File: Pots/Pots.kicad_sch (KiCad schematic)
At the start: 10 parts, among them J101 Conn_02x05_Odd_Even

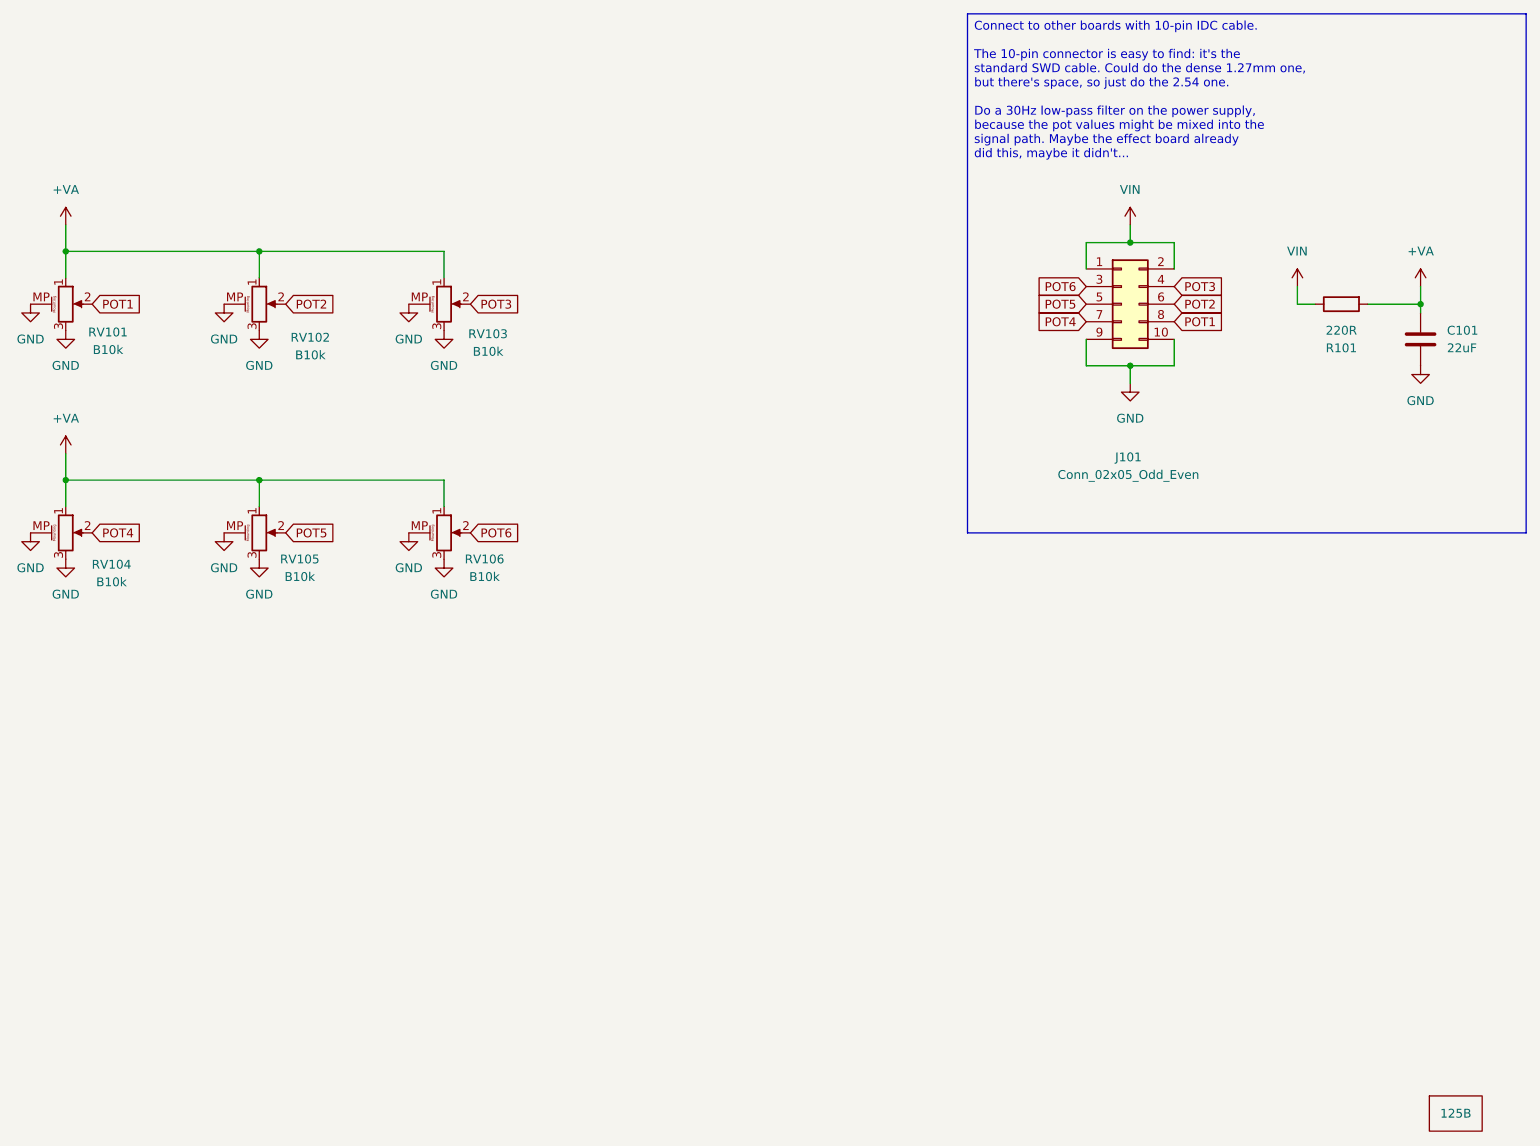
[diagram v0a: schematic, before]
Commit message: Move 3d models to footprint directory
I tried to deal with the kicad path handling with a 'TOPLEVEL'
environment variable, but it worked horribly badly and got out of sync
because kicad didn't really integrate very well with it.

So just live with the fact that you can only have per-project paths for
the symbol and footprint libraries, not for the 3D models.  kicad does
have the notion of "3D model paths", but they aren't per project.

It looks like the way to keep kicad happy and avoid too much confusion
is to just make the 3D models be part of the footprint library, and put
the STEP files in the same path.  I'll keep the original openscad models
in the 'Models' (and 'Enclosures') directories.

Let's see if this fixes my issues.

Also, this mixes in various other edits to the 1590B footprint in
particular, since I couldn't keep the regularly scheduled kicad noise
separate from the 'move things around' noise.  kicad likes to randomly
update the uuid's of various parts as something changes (or, as I
sometimes feel, even if nothing changes).

So this is not a particularly clean commit: this also moves the pot
locations up by 5mm in the 1590B enclosure because that's what I was
looking at when the potentiometer board stopped showing 3d models due to
path confusion.

Signed-off-by: Linus Torvalds <torvalds@linux-foundation.org>
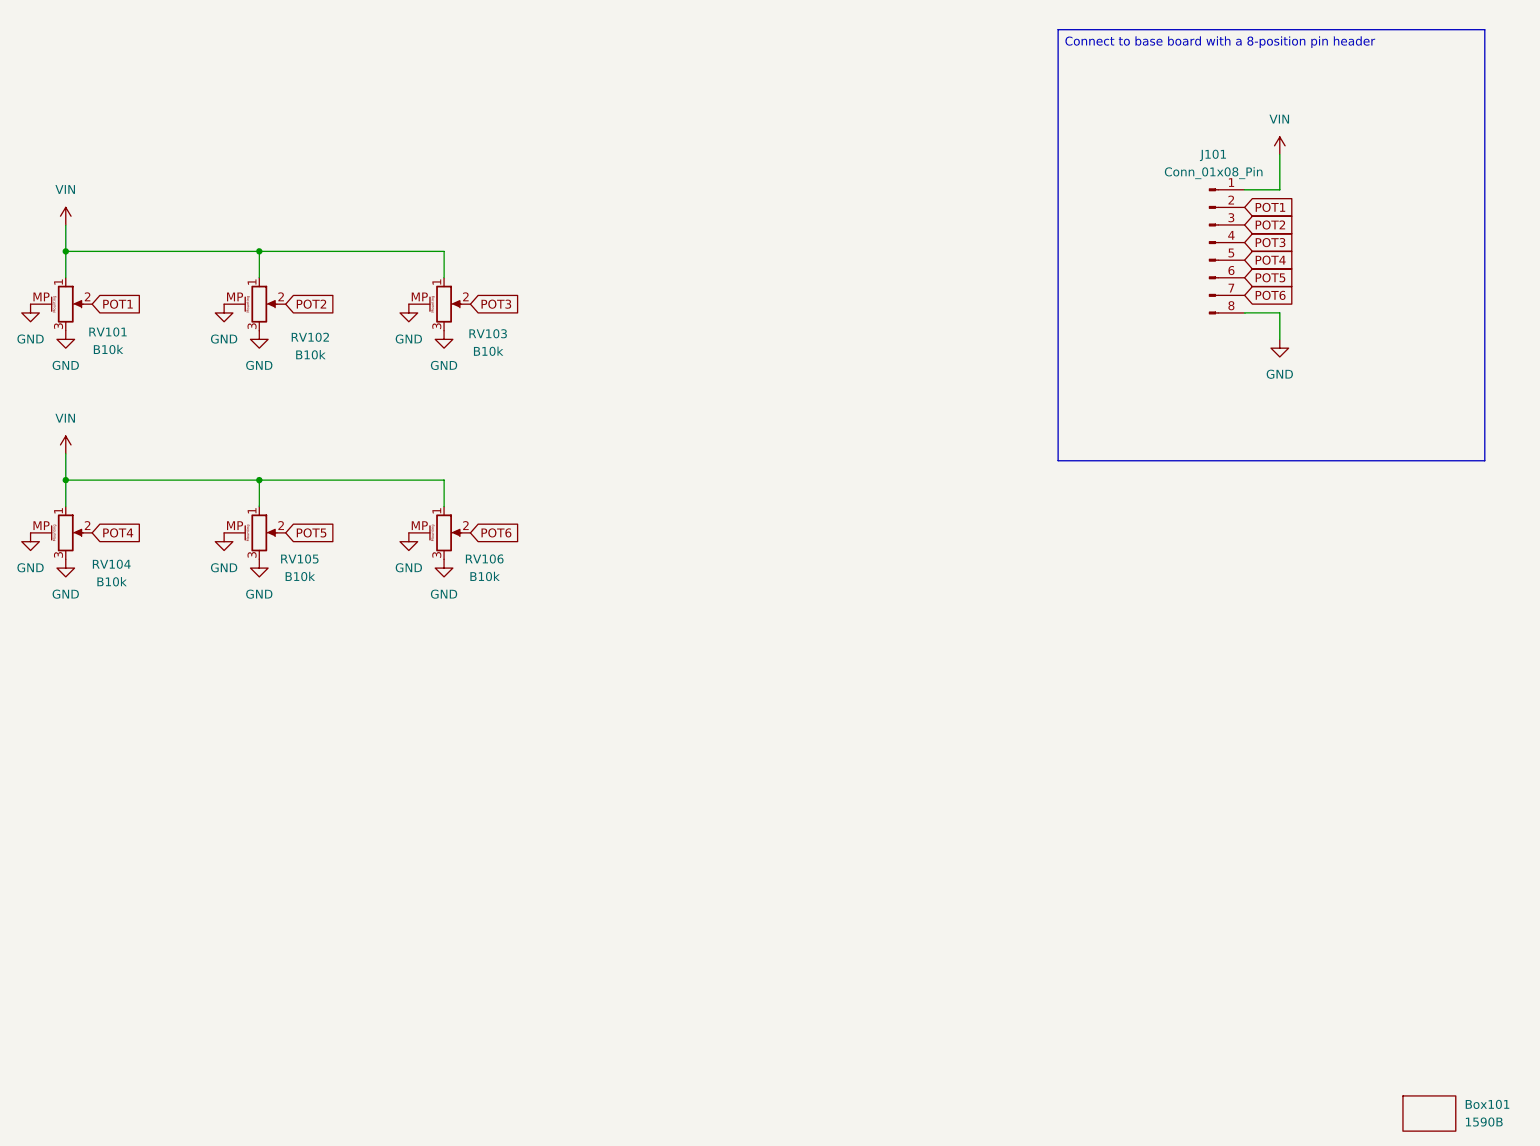
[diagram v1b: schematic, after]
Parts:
- removed Box101: 125B, Mylib:125B, symbol Mylib:Enclosure_125B
- removed C101: 22uF, Capacitor_SMD:C_1206_3216Metric, symbol Device:C
- removed J101: Conn_02x05_Odd_Even, Connector_PinHeader_1.27mm:PinHeader_2x05_P1.27mm_Vertical_SMD, symbol Connector_Generic:Conn_02x05_Odd_Even
- removed R101: 220R, Capacitor_SMD:C_0805_2012Metric, symbol Device:R
- added Box101: 1590B, Mylib:1590B, symbol Mylib:Enclosure_1590B
- added J101: Conn_01x08_Pin, Connector_PinHeader_2.54mm:PinHeader_1x08_P2.54mm_Vertical, symbol Connector:Conn_01x08_Pin
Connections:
- net +VA is gone; now on net VIN: RV101.1, RV102.1, RV103.1, RV104.1, RV105.1, RV106.1
- net GND: now also J101.8 (Pin_8)
- net POT1: now also J101.2 (Pin_2)
- net POT2: now also J101.3 (Pin_3)
- net POT3: now also J101.4 (Pin_4)
- net POT4: now also J101.5 (Pin_5)
- net POT5: now also J101.6 (Pin_6)
- net POT6: now also J101.7 (Pin_7)
- net VIN: now also J101.1 (Pin_1)

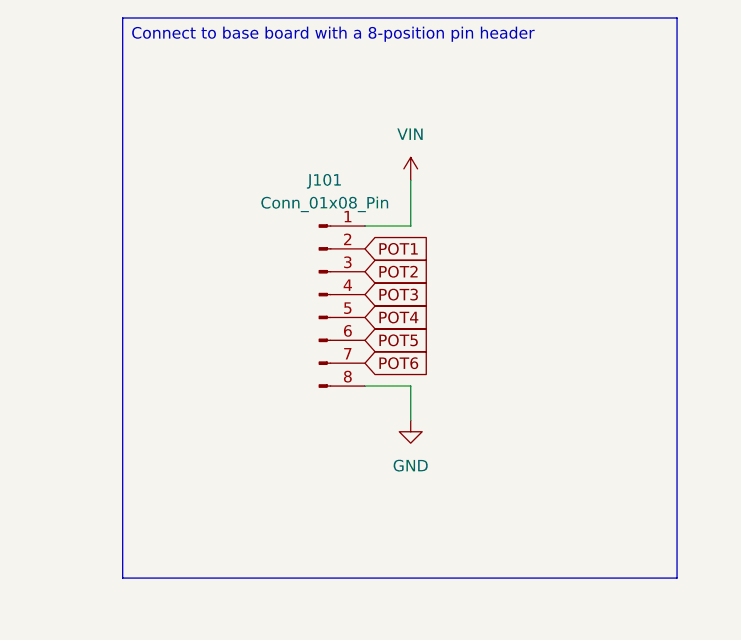
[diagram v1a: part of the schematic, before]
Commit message: Update potentiometer board
I think I have decided on 2x04 connector to the potentiometer board, at
least for now.  It's a bit more mechanically stable than a 1x08.

So redo the routing, do some via stitching, and put that thing in the
middle of the potentiometer board.  I think I'm almost ready for a 1590B
Daisy Seed board.

Signed-off-by: Linus Torvalds <torvalds@linux-foundation.org>
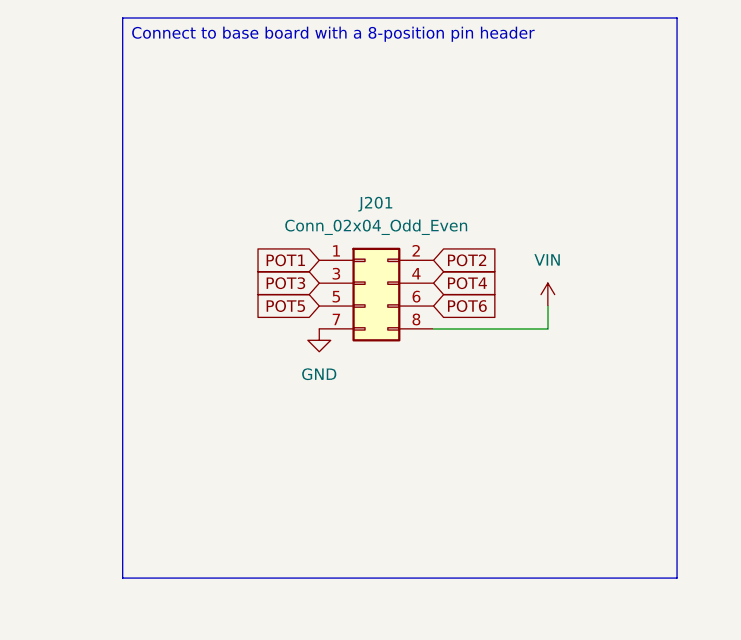
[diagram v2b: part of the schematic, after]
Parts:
- removed J101: Conn_01x08_Pin, Connector_PinHeader_2.54mm:PinHeader_1x08_P2.54mm_Vertical, symbol Connector:Conn_01x08_Pin
- added J201: Conn_02x04_Odd_Even, Connector_PinSocket_2.54mm:PinSocket_2x04_P2.54mm_Vertical, symbol Connector_Generic:Conn_02x04_Odd_Even
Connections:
- net GND: now also J201.7 (Pin_7)
- net POT1: now also J201.1 (Pin_1)
- net POT2: now also J201.2 (Pin_2)
- net POT3: now also J201.3 (Pin_3)
- net POT4: now also J201.4 (Pin_4)
- net POT5: now also J201.5 (Pin_5)
- net POT6: now also J201.6 (Pin_6)
- net VIN: now also J201.8 (Pin_8)

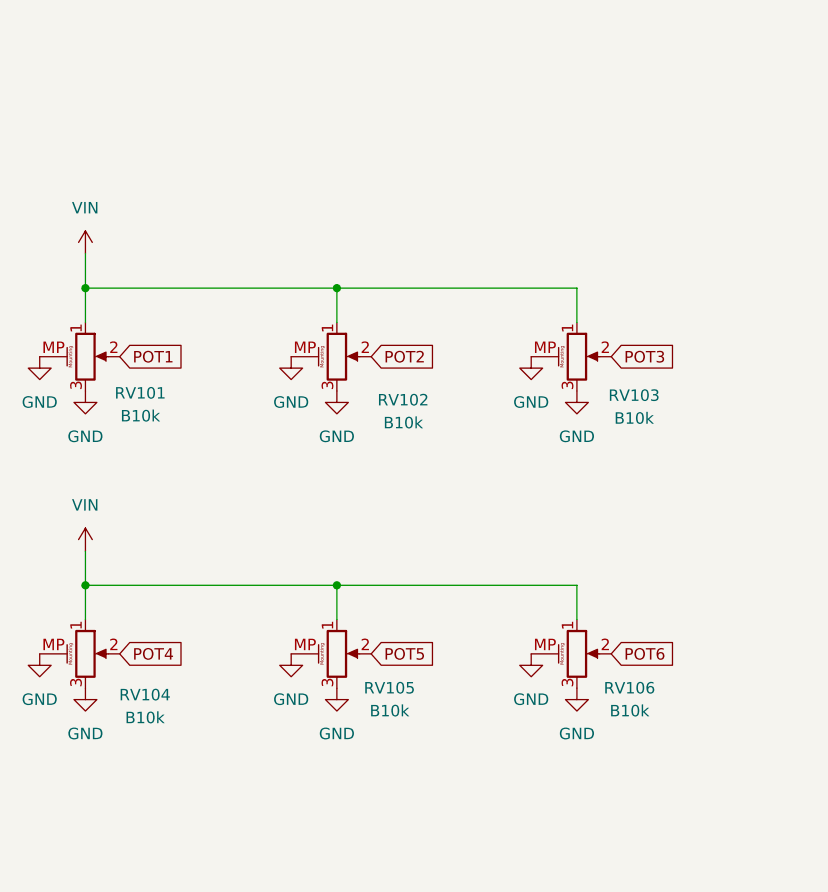
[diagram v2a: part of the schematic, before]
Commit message: Switch pots around for sane behavior
My 1590B test board works fine, but I was confused about the behavior of
the pots.  It turns out that for about the fifteenth time, I had them
the wrong way around.

Obviously the real cause is my incompetence, but I think it's made worse
by how the default symbol is laid out, with pin 1 at the top.  I then
mindlessly hook it up with positive rail at the top and ground at the
bottom, and the end result is the opposite of what the trivial
expectation is.

Not a biggie, this doesn't matter for my testing and could have been
fixed by just reprogramming the Daisy Seed too, but it's obviously a
"D'oh" moment.

Signed-off-by: Linus Torvalds <torvalds@linux-foundation.org>
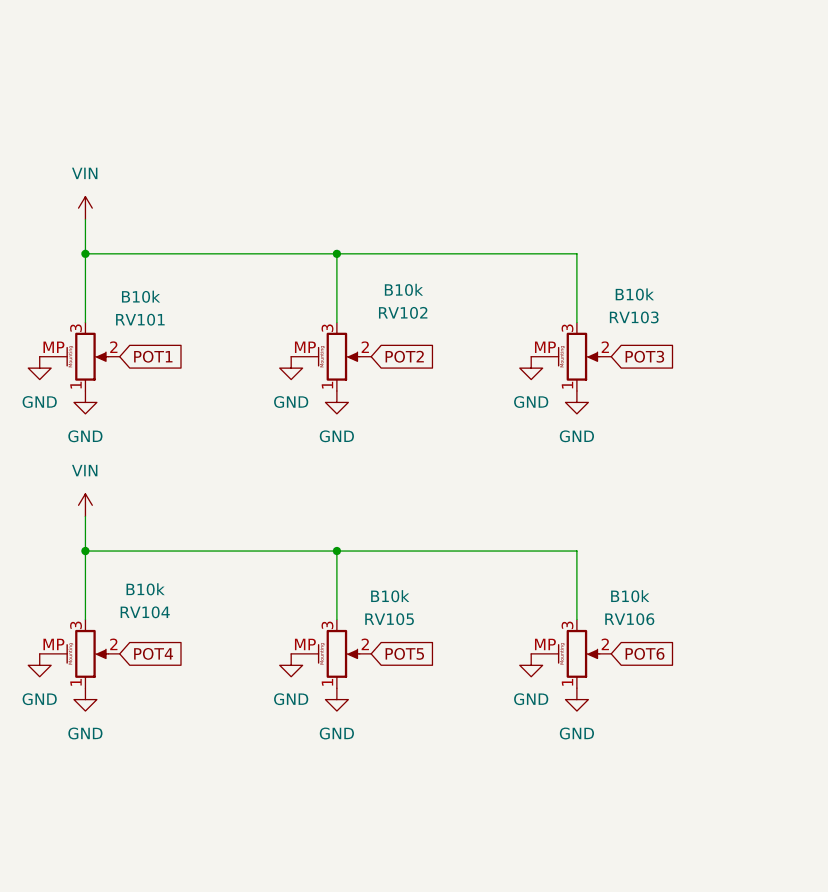
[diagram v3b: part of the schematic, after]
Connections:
- net GND: now also RV101.1, RV102.1, RV103.1, RV104.1, RV105.1, RV106.1; no longer RV101.3, RV102.3, RV103.3, RV104.3, RV105.3, RV106.3
- net VIN: now also RV101.3, RV102.3, RV103.3, RV104.3, RV105.3, RV106.3; no longer RV101.1, RV102.1, RV103.1, RV104.1, RV105.1, RV106.1
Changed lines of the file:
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@@
 	)
 	(junction
-		(at 97.79 49.53)
+		(at 69.85 78.74)
 		(diameter 0)
 		(color 0 0 0 0)
 	)
 	(junction
-		(at 69.85 49.53)
+		(at 69.85 45.72)
 		(diameter 0)
 		(color 0 0 0 0)
 	)
 	(junction
-		(at 97.79 82.55)
+		(at 97.79 78.74)
 		(diameter 0)
 		(color 0 0 0 0)
 	)
 	(junction
-		(at 69.85 82.55)
+		(at 97.79 45.72)
 		(diameter 0)
 		(color 0 0 0 0)
@@
 	(wire
 		(pts
-			(xy 69.85 82.55) (xy 69.85 86.36)
+			(xy 69.85 78.74) (xy 69.85 86.36)
 		)
 		(stroke
@@
 	(wire
 		(pts
-			(xy 124.46 49.53) (xy 124.46 53.34)
+			(xy 124.46 45.72) (xy 124.46 53.34)
 		)
 		(stroke
@@
 	(wire
 		(pts
-			(xy 69.85 78.74) (xy 69.85 82.55)
+			(xy 69.85 74.93) (xy 69.85 78.74)
 		)
 		(stroke
@@
 	(wire
 		(pts
-			(xy 97.79 82.55) (xy 97.79 86.36)
+			(xy 97.79 78.74) (xy 97.79 86.36)
 		)
 		(stroke
@@
 	(wire
 		(pts
-			(xy 69.85 49.53) (xy 69.85 53.34)
+			(xy 97.79 45.72) (xy 124.46 45.72)
 		)
 		(stroke
@@
 	(wire
 		(pts
-			(xy 97.79 49.53) (xy 124.46 49.53)
+			(xy 97.79 45.72) (xy 97.79 53.34)
 		)
 		(stroke
@@
 	(wire
 		(pts
-			(xy 69.85 82.55) (xy 97.79 82.55)
+			(xy 69.85 78.74) (xy 97.79 78.74)
 		)
 		(stroke
@@
 	(wire
 		(pts
-			(xy 124.46 82.55) (xy 124.46 86.36)
+			(xy 124.46 78.74) (xy 124.46 86.36)
 		)
 		(stroke
@@
 	(wire
 		(pts
-			(xy 69.85 49.53) (xy 97.79 49.53)
+			(xy 69.85 45.72) (xy 97.79 45.72)
 		)
 		(stroke
@@
 	(wire
 		(pts
-			(xy 69.85 45.72) (xy 69.85 49.53)
+			(xy 69.85 41.91) (xy 69.85 45.72)
 		)
 		(stroke
@@
 	(wire
 		(pts
-			(xy 97.79 49.53) (xy 97.79 53.34)
+			(xy 97.79 78.74) (xy 124.46 78.74)
 		)
 		(stroke
@@
 	(wire
 		(pts
-			(xy 97.79 82.55) (xy 124.46 82.55)
+			(xy 69.85 45.72) (xy 69.85 53.34)
 		)
 		(stroke
@@
 	(symbol
 		(lib_id "power:+3.3VA")
-		(at 69.85 78.74 0)
+		(at 69.85 74.93 0)
 		(unit 1)
 		(exclude_from_sim no)
@@
 		(fields_autoplaced yes)
 		(property "Reference" "#PWR0113"
-			(at 69.85 82.55 0)
+			(at 69.85 78.74 0)
 			(effects
 				(font
@@
 		)
 		(property "Value" "VIN"
-			(at 69.85 73.66 0)
+			(at 69.85 69.85 0)
 			(effects
 				(font
@@
 		)
 		(property "Footprint" ""
-			(at 69.85 78.74 0)
+			(at 69.85 74.93 0)
 			(effects
 				(font
@@
 		)
 		(property "Datasheet" ""
-			(at 69.85 78.74 0)
+			(at 69.85 74.93 0)
 			(effects
 				(font
@@
 		)
 		(property "Description" "Power symbol creates a global label with name \"+3.3VA\""
-			(at 69.85 78.74 0)
+			(at 69.85 74.93 0)
 			(effects
 				(font
@@
 		(lib_id "Device:R_Potentiometer_MountingPin")
 		(at 69.85 57.15 0)
+		(mirror x)
 		(unit 1)
 		(exclude_from_sim no)
@@
 		(dnp no)
 		(property "Reference" "RV101"
-			(at 75.946 61.214 0)
+			(at 75.946 53.086 0)
 			(effects
 				(font
@@
 		)
 		(property "Value" "B10k"
-			(at 75.946 63.754 0)
+			(at 75.946 50.546 0)
 			(effects
 				(font
@@
 	(symbol
 		(lib_id "power:+3.3VA")
-		(at 69.85 45.72 0)
+		(at 69.85 41.91 0)
 		(unit 1)
 		(exclude_from_sim no)
@@
 		(fields_autoplaced yes)
 		(property "Reference" "#PWR0101"
-			(at 69.85 49.53 0)
+			(at 69.85 45.72 0)
 			(effects
 				(font
@@
 		)
 		(property "Value" "VIN"
-			(at 69.85 40.64 0)
+			(at 69.85 36.83 0)
 			(effects
 				(font
@@
 		)
 		(property "Footprint" ""
-			(at 69.85 45.72 0)
+			(at 69.85 41.91 0)
 			(effects
 				(font
@@
 		)
 		(property "Datasheet" ""
-			(at 69.85 45.72 0)
+			(at 69.85 41.91 0)
 			(effects
 				(font
@@
 		)
 		(property "Description" "Power symbol creates a global label with name \"+3.3VA\""
-			(at 69.85 45.72 0)
+			(at 69.85 41.91 0)
 			(effects
 				(font
@@
 		(lib_id "Device:R_Potentiometer_MountingPin")
 		(at 124.46 57.15 0)
+		(mirror x)
 		(unit 1)
 		(exclude_from_sim no)
@@
 		(dnp no)
 		(property "Reference" "RV103"
-			(at 130.81 61.468 0)
+			(at 130.81 52.832 0)
 			(effects
 				(font
@@
 		)
 		(property "Value" "B10k"
-			(at 130.81 64.008 0)
+			(at 130.81 50.292 0)
 			(effects
 				(font
@@
 		(lib_id "Device:R_Potentiometer_MountingPin")
 		(at 97.79 57.15 0)
+		(mirror x)
 		(unit 1)
 		(exclude_from_sim no)
@@
 		(dnp no)
 		(property "Reference" "RV102"
-			(at 105.156 61.976 0)
+			(at 105.156 52.324 0)
 			(effects
 				(font
@@
 		)
 		(property "Value" "B10k"
-			(at 105.156 64.516 0)
+			(at 105.156 49.784 0)
 			(effects
 				(font
@@
 		(lib_id "Device:R_Potentiometer_MountingPin")
 		(at 69.85 90.17 0)
+		(mirror x)
 		(unit 1)
 		(exclude_from_sim no)
@@
 		(dnp no)
 		(property "Reference" "RV104"
-			(at 76.454 94.742 0)
+			(at 76.454 85.598 0)
 			(effects
 				(font
@@
 		)
 		(property "Value" "B10k"
-			(at 76.454 97.282 0)
+			(at 76.454 83.058 0)
 			(effects
 				(font
@@
 		(lib_id "Device:R_Potentiometer_MountingPin")
 		(at 124.46 90.17 0)
+		(mirror x)
 		(unit 1)
 		(exclude_from_sim no)
@@
 		(dnp no)
 		(property "Reference" "RV106"
-			(at 130.302 93.98 0)
+			(at 130.302 86.36 0)
 			(effects
 				(font
@@
 		)
 		(property "Value" "B10k"
-			(at 130.302 96.52 0)
+			(at 130.302 83.82 0)
 			(effects
 				(font
@@
 		(lib_id "Device:R_Potentiometer_MountingPin")
 		(at 97.79 90.17 0)
+		(mirror x)
 		(unit 1)
 		(exclude_from_sim no)
@@
 		(dnp no)
 		(property "Reference" "RV105"
-			(at 103.632 93.98 0)
+			(at 103.632 86.36 0)
 			(effects
 				(font
@@
 		)
 		(property "Value" "B10k"
-			(at 103.632 96.52 0)
-			(effects
-				(font
+			(at 103.632 83.82 0)
+			(effects
+				(font
